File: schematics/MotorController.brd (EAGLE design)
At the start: 127 x 96.2 mm, 37 parts, among them IC1 7805, Q1 BC307

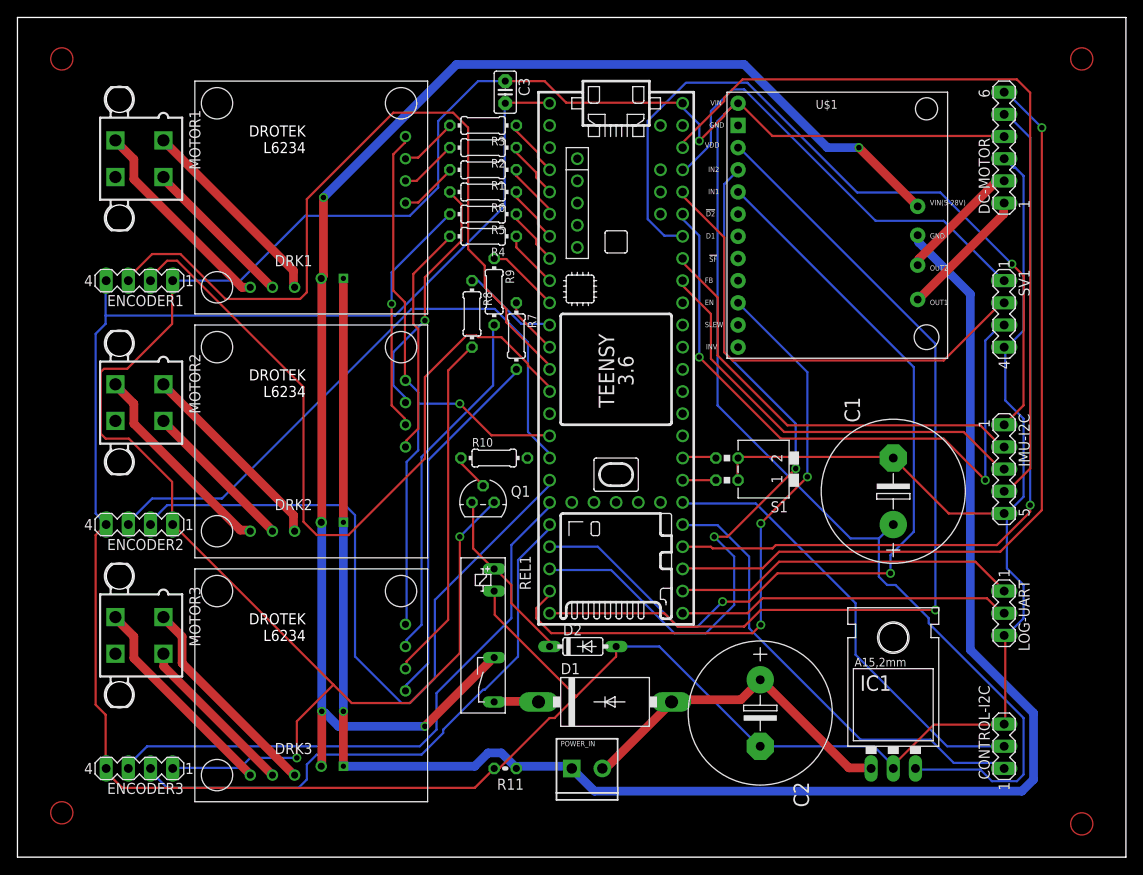
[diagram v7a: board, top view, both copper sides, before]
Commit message: Motor too weak and gets too hot. Mist.
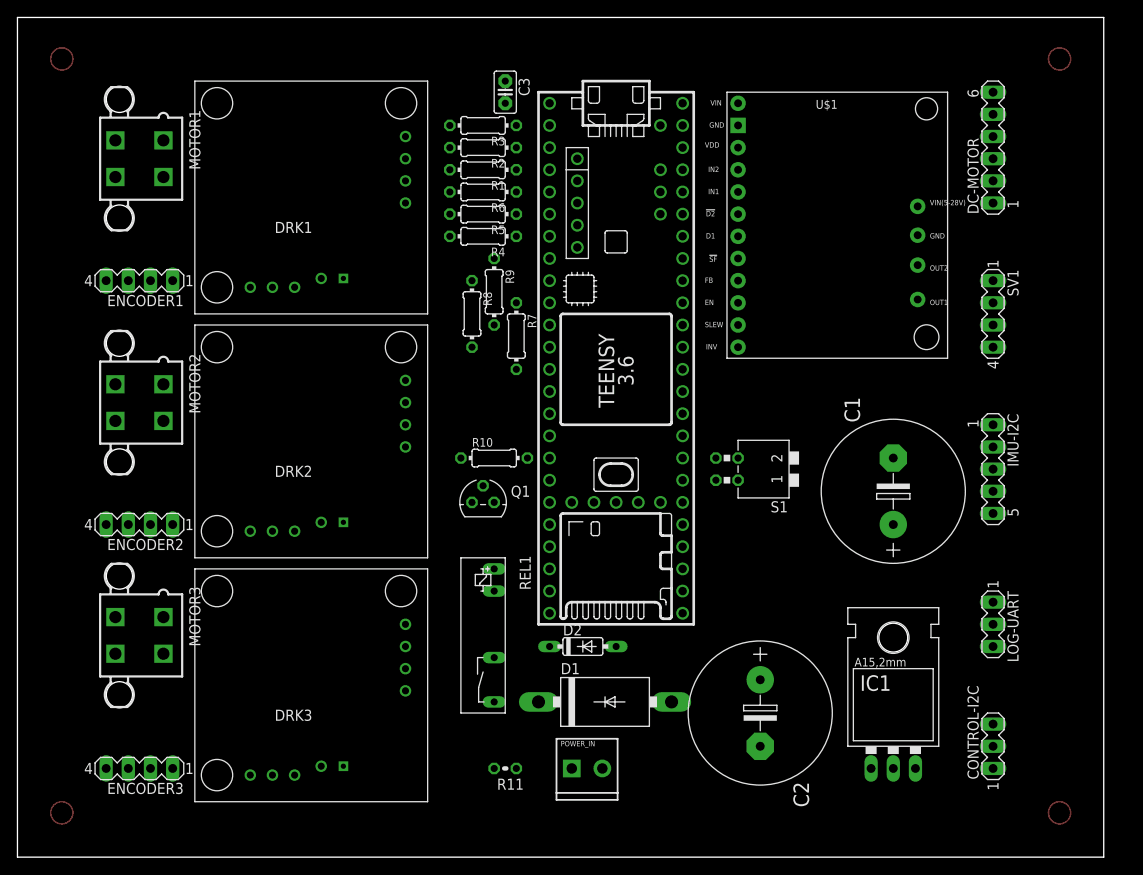
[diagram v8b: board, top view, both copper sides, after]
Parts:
- moved LOG-UART 1.80 mm to (39.4, 17.8)
- moved CONTROL-I2C 1.27 mm to (39.4, 3.81)
- moved DC-MOTOR 1.27 mm to (39.4, 72.4)
- moved IMU-I2C 1.27 mm to (39.4, 35.6)
- moved SV1 1.27 mm to (39.4, 53.3)
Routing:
- net GND: track 368.9 -> 0.00 mm
- net VCC: track 353.1 -> 0.00 mm, vias 3 -> 0
- net LIPO-GND: track 206.0 -> 0.00 mm, vias 1 -> 0
- net LIPO-VDD: track 170.2 -> 0.00 mm, vias 4 -> 0
- net N$41: track 108.0 -> 0.00 mm, vias 1 -> 0
- net N$44: track 98.5 -> 0.00 mm, vias 2 -> 0
- net WH_ENC_B: track 93.9 -> 0.00 mm, vias 1 -> 0
- net N$46: track 91.4 -> 0.00 mm
- net N$33: track 89.9 -> 0.00 mm
- net Y_ENC_A: track 88.6 -> 0.00 mm, vias 1 -> 0
- net N$48: track 88.1 -> 0.00 mm, vias 1 -> 0
- net N$34: track 87.0 -> 0.00 mm
- net N$47: track 85.2 -> 0.00 mm, vias 2 -> 0
- net N$36: track 81.9 -> 0.00 mm
- net N$10: track 75.0 -> 0.00 mm, vias 1 -> 0
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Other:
- board size 127 x 96.2 mm -> 124.4 x 96.2 mm
